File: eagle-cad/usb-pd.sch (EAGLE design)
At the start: 41 parts, among them Q1 CERAMIC_RESONATOR_SMD6M00G53Z, U1 ATMEGA328-AU

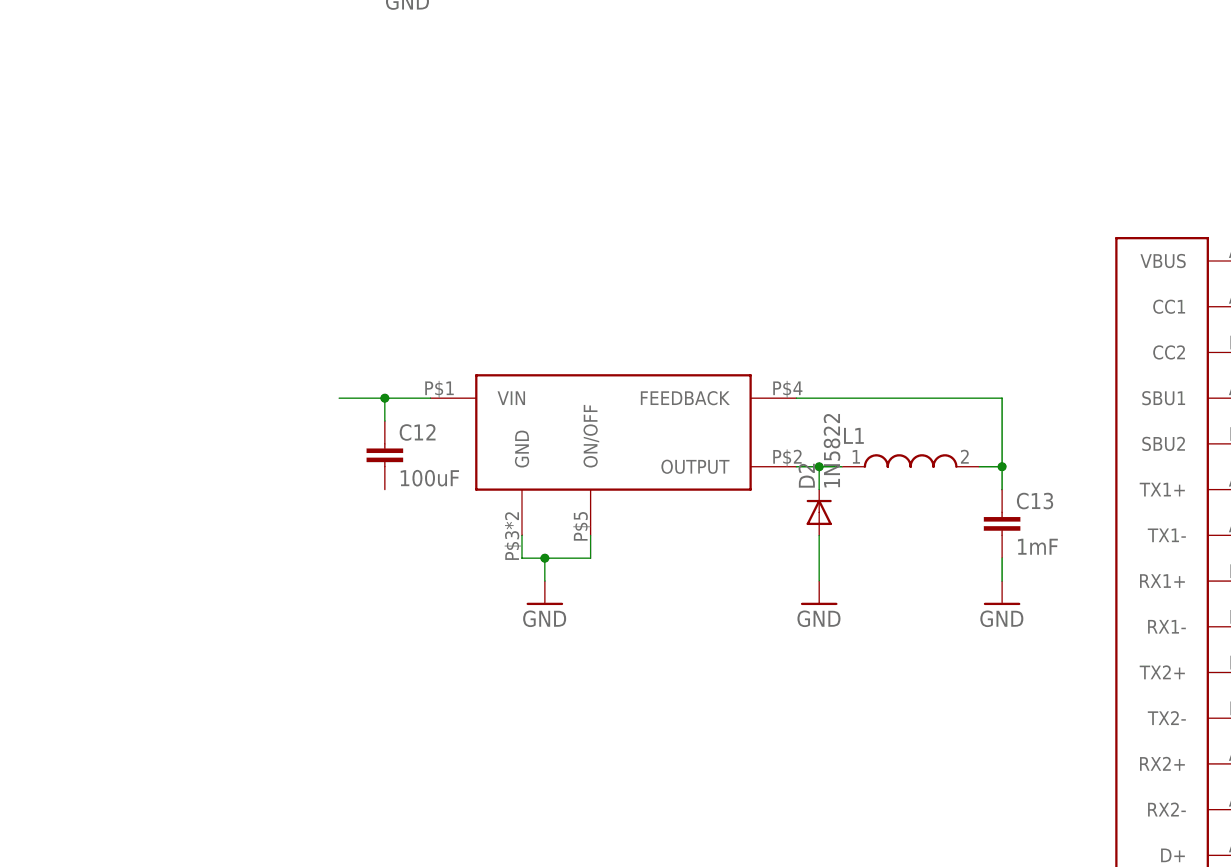
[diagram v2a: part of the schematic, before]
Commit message: Added a n-channel power MOSFET to serve as controlling power FET for 5V buck. Definitely needs review
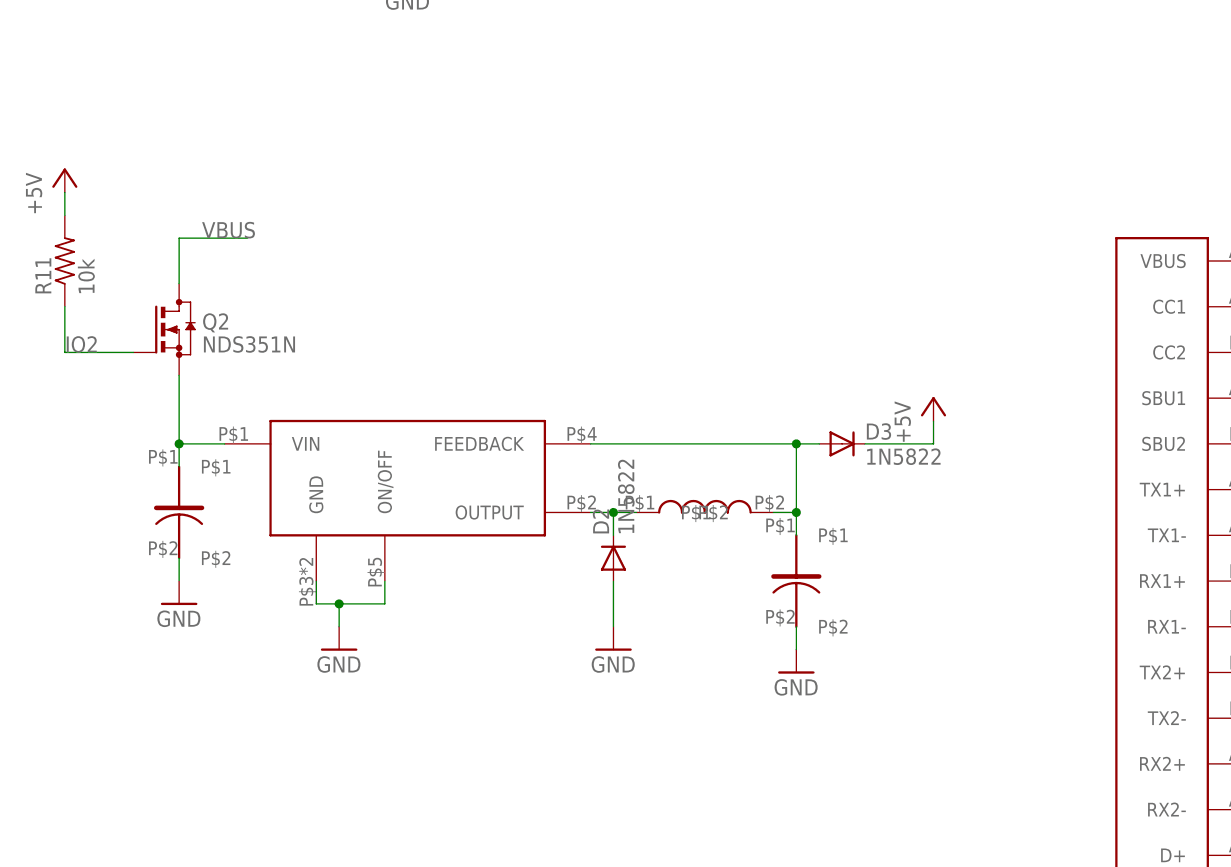
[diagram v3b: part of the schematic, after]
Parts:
- removed C12: 100uF, rcl:C-EUC0805
- removed L1: (no value), EagleLibrary_Wuerth_Elektronik_eiSos_rev16a:WE-RFI_0805
- added D3: 1N5822, diode:1N5400
- added Q2: NDS351N, transistor-small-signal:BSS123
- added R11: 10k, rcl:R-US_R0805
- added U$7: WEURTH-784771101, usb-pd:WEURTH-784771101
- added U$8: UWT1V101MCL1GS, usb-pd:UWT1V101MCL1GS
- C13: value 1mF -> AVE108M10G24T-F; device rcl:C-EUC0805 -> usb-pd:AVE108M10G24T-F
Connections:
- net +5V: now also D3.C, R11.2
- net GND: now also C13.P$2, U$8.P$2; no longer C13.2
- net IO2: now also Q2.G, R11.1
- net N$1: now also Q2.S, U$8.P$1; no longer C12.1
- net N$15: now also C13.P$1, D3.A, U$7.P$2; no longer C13.1, L1.2
- net N$9: now also U$7.P$1; no longer L1.1
- net VBUS: now also Q2.D
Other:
- moved on the sheet: D2
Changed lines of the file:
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@@
 <part name="+3V3" library="supply1" deviceset="+3V3" device=""/>
 <part name="U$6" library="usb-pd" deviceset="TI-LM2576-5.0" device=""/>
-<part name="C12" library="rcl" deviceset="C-EU" device="C0805" value="100uF"/>
 <part name="GND17" library="supply1" deviceset="GND" device=""/>
-<part name="C13" library="rcl" deviceset="C-EU" device="C0805" value="1mF"/>
 <part name="GND18" library="supply1" deviceset="GND" device=""/>
 <part name="D2" library="diode" deviceset="1N5400" device="" value="1N5822"/>
 <part name="GND19" library="supply1" deviceset="GND" device=""/>
-<part name="L1" library="EagleLibrary_Wuerth_Elektronik_eiSos_rev16a" deviceset="WE-RFI" device="_0805"/>
+<part name="D3" library="diode" deviceset="1N5400" device="" value="1N5822"/>
+<part name="P+12" library="supply1" deviceset="+5V" device=""/>
+<part name="U$7" library="usb-pd" deviceset="WEURTH-784771101" device=""/>
+<part name="C13" library="usb-pd" deviceset="AVE108M10G24T-F" device=""/>
+<part name="GND20" library="supply1" deviceset="GND" device=""/>
+<part name="U$8" library="usb-pd" deviceset="UWT1V101MCL1GS" device=""/>
+<part name="Q2" library="transistor-small-signal" deviceset="BSS123" device="" value="NDS351N"/>
+<part name="P+13" library="supply1" deviceset="+5V" device=""/>
+<part name="R11" library="rcl" deviceset="R-US_" device="R0805" value="10k"/>
 </parts>
 <sheets>
@@
 <instance part="P+11" gate="1" x="208.28" y="132.08"/>
 <instance part="+3V3" gate="G$1" x="215.9" y="132.08"/>
-<instance part="U$6" gate="G$1" x="-76.2" y="60.96"/>
-<instance part="C12" gate="G$1" x="-96.52" y="58.42"/>
-<instance part="GND17" gate="1" x="-78.74" y="40.64"/>
-<instance part="C13" gate="G$1" x="-27.94" y="50.8"/>
-<instance part="GND18" gate="1" x="-27.94" y="40.64"/>
-<instance part="D2" gate="1" x="-48.26" y="50.8" rot="R90"/>
-<instance part="GND19" gate="1" x="-48.26" y="40.64"/>
-<instance part="L1" gate="G$1" x="-38.1" y="55.88"/>
+<instance part="U$6" gate="G$1" x="-99.06" y="55.88"/>
+<instance part="GND17" gate="1" x="-101.6" y="35.56"/>
+<instance part="GND18" gate="1" x="-50.8" y="33.02"/>
+<instance part="D2" gate="1" x="-71.12" y="45.72" rot="R90"/>
+<instance part="GND19" gate="1" x="-71.12" y="35.56"/>
+<instance part="D3" gate="1" x="-45.72" y="58.42"/>
+<instance part="P+12" gate="1" x="-35.56" y="63.5"/>
+<instance part="U$7" gate="G$1" x="-60.96" y="50.8"/>
+<instance part="C13" gate="G$1" x="-50.8" y="45.72"/>
+<instance part="GND20" gate="1" x="-119.38" y="40.64"/>
+<instance part="U$8" gate="G$1" x="-119.38" y="53.34"/>
+<instance part="Q2" gate="G$1" x="-119.38" y="71.12"/>
+<instance part="P+13" gate="1" x="-132.08" y="88.9"/>
+<instance part="R11" gate="G$1" x="-132.08" y="78.74" rot="R90"/>
 </instances>
 <busses>
@@
 <wire x1="208.28" y1="124.46" x2="208.28" y2="129.54" width="0.1524" layer="91"/>
 </segment>
+<segment>
+<pinref part="D3" gate="1" pin="C"/>
+<wire x1="-43.18" y1="58.42" x2="-35.56" y2="58.42" width="0.1524" layer="91"/>
+<pinref part="P+12" gate="1" pin="+5V"/>
+<wire x1="-35.56" y1="58.42" x2="-35.56" y2="60.96" width="0.1524" layer="91"/>
+</segment>
+<segment>
+<pinref part="R11" gate="G$1" pin="2"/>
+<pinref part="P+13" gate="1" pin="+5V"/>
+<wire x1="-132.08" y1="83.82" x2="-132.08" y2="86.36" width="0.1524" layer="91"/>
+</segment>
 </net>
 <net name="GND" class="0">
@@
 <segment>
 <pinref part="U$6" gate="G$1" pin="GND"/>
-<wire x1="-81.28" y1="48.26" x2="-81.28" y2="45.72" width="0.1524" layer="91"/>
+<wire x1="-104.14" y1="43.18" x2="-104.14" y2="40.64" width="0.1524" layer="91"/>
 <pinref part="GND17" gate="1" pin="GND"/>
-<wire x1="-81.28" y1="45.72" x2="-78.74" y2="45.72" width="0.1524" layer="91"/>
-<wire x1="-78.74" y1="45.72" x2="-78.74" y2="43.18" width="0.1524" layer="91"/>
-<junction x="-78.74" y="45.72"/>
+<wire x1="-104.14" y1="40.64" x2="-101.6" y2="40.64" width="0.1524" layer="91"/>
+<wire x1="-101.6" y1="40.64" x2="-101.6" y2="38.1" width="0.1524" layer="91"/>
+<junction x="-101.6" y="40.64"/>
 <pinref part="U$6" gate="G$1" pin="ON/OFF"/>
-<wire x1="-73.66" y1="48.26" x2="-73.66" y2="45.72" width="0.1524" layer="91"/>
-<wire x1="-73.66" y1="45.72" x2="-78.74" y2="45.72" width="0.1524" layer="91"/>
+<wire x1="-96.52" y1="43.18" x2="-96.52" y2="40.64" width="0.1524" layer="91"/>
+<wire x1="-96.52" y1="40.64" x2="-101.6" y2="40.64" width="0.1524" layer="91"/>
 </segment>
 <segment>
 <pinref part="GND18" gate="1" pin="GND"/>
-<pinref part="C13" gate="G$1" pin="2"/>
-<wire x1="-27.94" y1="43.18" x2="-27.94" y2="45.72" width="0.1524" layer="91"/>
+<wire x1="-50.8" y1="35.56" x2="-50.8" y2="38.1" width="0.1524" layer="91"/>
+<pinref part="C13" gate="G$1" pin="P$2"/>
 </segment>
 <segment>
 <pinref part="D2" gate="1" pin="A"/>
 <pinref part="GND19" gate="1" pin="GND"/>
-<wire x1="-48.26" y1="48.26" x2="-48.26" y2="43.18" width="0.1524" layer="91"/>
+<wire x1="-71.12" y1="43.18" x2="-71.12" y2="38.1" width="0.1524" layer="91"/>
+</segment>
+<segment>
+<pinref part="GND20" gate="1" pin="GND"/>
+<wire x1="-119.38" y1="43.18" x2="-119.38" y2="45.72" width="0.1524" layer="91"/>
+<pinref part="U$8" gate="G$1" pin="P$2"/>
 </segment>
 </net>
@@
 <label x="198.12" y="15.24" size="1.778" layer="95"/>
 </segment>
+<segment>
+<pinref part="R11" gate="G$1" pin="1"/>
+<wire x1="-132.08" y1="73.66" x2="-132.08" y2="68.58" width="0.1524" layer="91"/>
+<pinref part="Q2" gate="G$1" pin="G"/>
+<wire x1="-132.08" y1="68.58" x2="-124.46" y2="68.58" width="0.1524" layer="91"/>
+<label x="-132.08" y="68.58" size="1.778" layer="95"/>
+</segment>
 </net>
 <net name="IO3" class="0">
@@
 <label x="218.44" y="116.84" size="1.778" layer="95"/>
 </segment>
+<segment>
+<pinref part="Q2" gate="G$1" pin="D"/>
+<wire x1="-119.38" y1="76.2" x2="-119.38" y2="81.28" width="0.1524" layer="91"/>
+<wire x1="-119.38" y1="81.28" x2="-111.76" y2="81.28" width="0.1524" layer="91"/>
+<label x="-116.84" y="81.28" size="1.778" layer="95"/>
+</segment>
 </net>
 <net name="N$1" class="0">
 <segment>
 <pinref part="U$6" gate="G$1" pin="VIN"/>
-<pinref part="C12" gate="G$1" pin="1"/>
-<wire x1="-91.44" y1="63.5" x2="-96.52" y2="63.5" width="0.1524" layer="91"/>
-<wire x1="-96.52" y1="63.5" x2="-96.52" y2="60.96" width="0.1524" layer="91"/>
-<wire x1="-96.52" y1="63.5" x2="-101.6" y2="63.5" width="0.1524" layer="91"/>
-<junction x="-96.52" y="63.5"/>
+<wire x1="-114.3" y1="58.42" x2="-119.38" y2="58.42" width="0.1524" layer="91"/>
+<pinref part="U$8" gate="G$1" pin="P$1"/>
+<wire x1="-119.38" y1="55.88" x2="-119.38" y2="58.42" width="0.1524" layer="91"/>
+<pinref part="Q2" gate="G$1" pin="S"/>
+<wire x1="-119.38" y1="58.42" x2="-119.38" y2="66.04" width="0.1524" layer="91"/>
+<junction x="-119.38" y="58.42"/>
 </segment>
 </net>
 <net name="N$15" class="0">
 <segment>
-<pinref part="C13" gate="G$1" pin="1"/>
-<wire x1="-27.94" y1="55.88" x2="-27.94" y2="53.34" width="0.1524" layer="91"/>
-<junction x="-27.94" y="55.88"/>
+<wire x1="-50.8" y1="50.8" x2="-50.8" y2="48.26" width="0.1524" layer="91"/>
+<junction x="-50.8" y="50.8"/>
 <pinref part="U$6" gate="G$1" pin="FEEDBACK"/>
-<wire x1="-50.8" y1="63.5" x2="-27.94" y2="63.5" width="0.1524" layer="91"/>
-<wire x1="-27.94" y1="63.5" x2="-27.94" y2="55.88" width="0.1524" layer="91"/>
-<pinref part="L1" gate="G$1" pin="2"/>
-<wire x1="-30.48" y1="55.88" x2="-27.94" y2="55.88" width="0.1524" layer="91"/>
+<wire x1="-73.66" y1="58.42" x2="-50.8" y2="58.42" width="0.1524" layer="91"/>
+<wire x1="-50.8" y1="58.42" x2="-50.8" y2="50.8" width="0.1524" layer="91"/>
+<wire x1="-53.34" y1="50.8" x2="-50.8" y2="50.8" width="0.1524" layer="91"/>
+<junction x="-50.8" y="58.42"/>
+<pinref part="D3" gate="1" pin="A"/>
+<wire x1="-48.26" y1="58.42" x2="-50.8" y2="58.42" width="0.1524" layer="91"/>
+<pinref part="U$7" gate="G$1" pin="P$2"/>
+<pinref part="C13" gate="G$1" pin="P$1"/>
 </segment>
 </net>
@@
 <pinref part="U$6" gate="G$1" pin="OUTPUT"/>
 <pinref part="D2" gate="1" pin="C"/>
-<wire x1="-50.8" y1="55.88" x2="-48.26" y2="55.88" width="0.1524" layer="91"/>
-<wire x1="-48.26" y1="55.88" x2="-48.26" y2="53.34" width="0.1524" layer="91"/>
-<junction x="-48.26" y="55.88"/>
-<pinref part="L1" gate="G$1" pin="1"/>
-<wire x1="-48.26" y1="55.88" x2="-45.72" y2="55.88" width="0.1524" layer="91"/>
-</segment>
-</net>
+<wire x1="-73.66" y1="50.8" x2="-71.12" y2="50.8" width="0.1524" layer="91"/>
+<wire x1="-71.12" y1="50.8" x2="-71.12" y2="48.26" width="0.1524" layer="91"/>
+<junction x="-71.12" y="50.8"/>
+<wire x1="-71.12" y1="50.8" x2="-68.58" y2="50.8" width="0.1524" layer="91"/>
+<pinref part="U$7" gate="G$1" pin="P$1"/>
+</segment>
+</net>

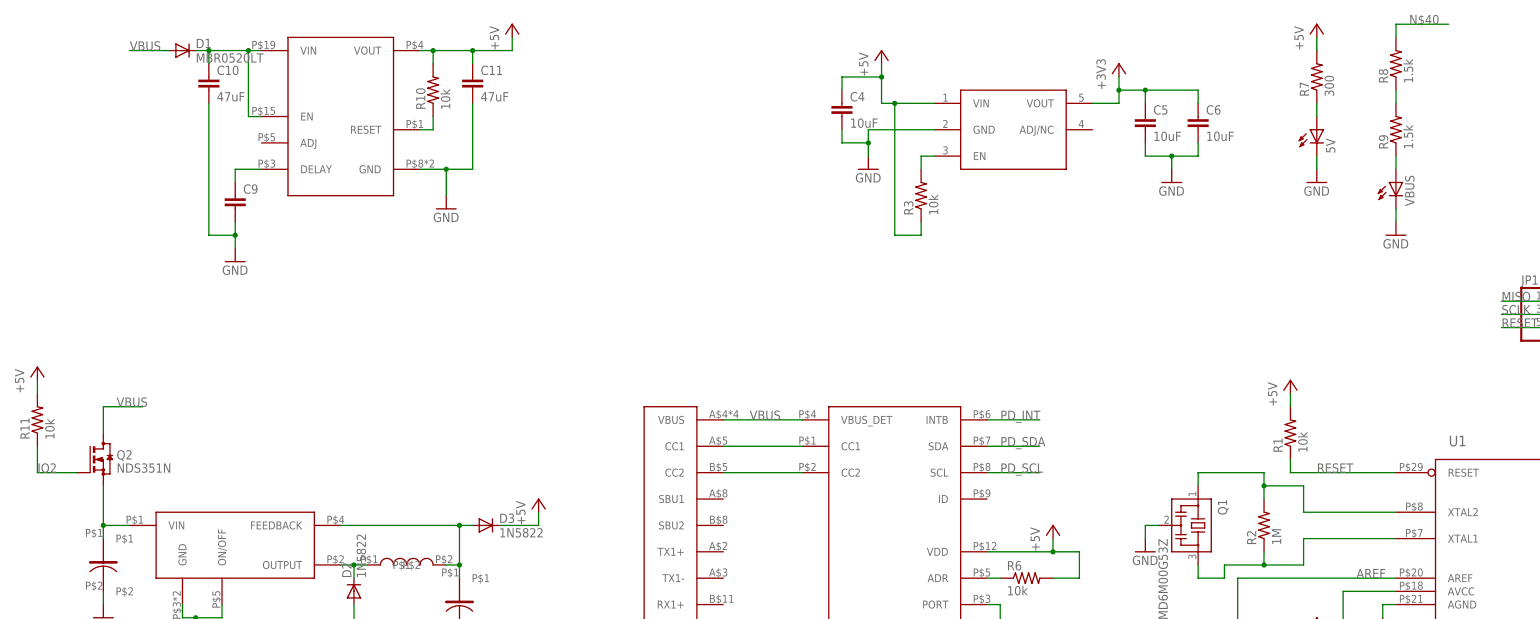
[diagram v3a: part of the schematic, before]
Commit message: switched to p-channel because I'm dumb
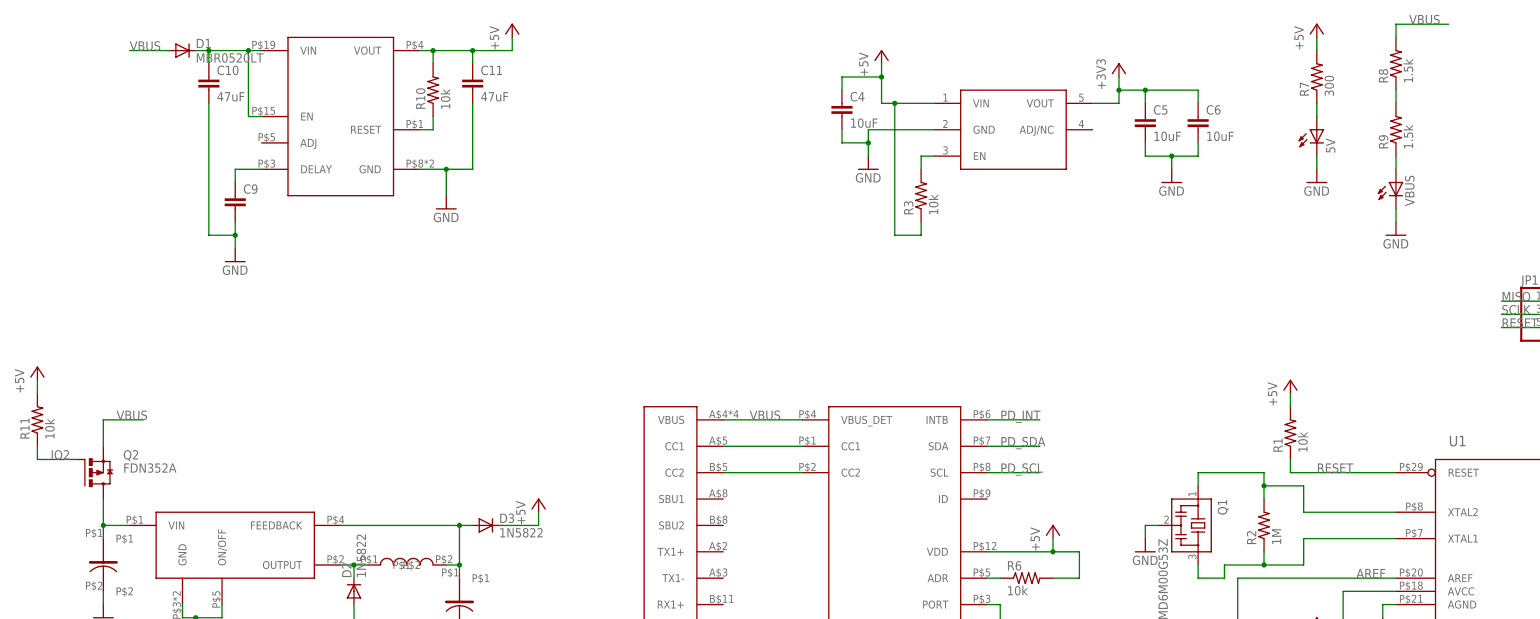
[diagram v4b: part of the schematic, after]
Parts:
- Q2: value NDS351N -> FDN352A; device transistor-small-signal:BSS123 -> transistor-power:FDN360P
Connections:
- net N$1: now also Q2.D; no longer Q2.S
- net N$40: no longer R8.2
- net VBUS: now also Q2.S, R8.2; no longer Q2.D
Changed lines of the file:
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@@
 <part name="GND20" library="supply1" deviceset="GND" device=""/>
 <part name="U$8" library="usb-pd" deviceset="UWT1V101MCL1GS" device=""/>
-<part name="Q2" library="transistor-small-signal" deviceset="BSS123" device="" value="NDS351N"/>
 <part name="P+13" library="supply1" deviceset="+5V" device=""/>
 <part name="R11" library="rcl" deviceset="R-US_" device="R0805" value="10k"/>
+<part name="Q2" library="transistor-power" deviceset="FDN360P" device="" value="FDN352A"/>
 </parts>
 <sheets>
@@
 <instance part="GND20" gate="1" x="-119.38" y="40.64"/>
 <instance part="U$8" gate="G$1" x="-119.38" y="53.34"/>
-<instance part="Q2" gate="G$1" x="-119.38" y="71.12"/>
 <instance part="P+13" gate="1" x="-132.08" y="88.9"/>
 <instance part="R11" gate="G$1" x="-132.08" y="78.74" rot="R90"/>
+<instance part="Q2" gate="G$1" x="-121.92" y="68.58"/>
 </instances>
 <busses>
@@
 <net name="N$40" class="0">
 <segment>
-<pinref part="R8" gate="G$1" pin="2"/>
-<wire x1="129.54" y1="152.4" x2="129.54" y2="154.94" width="0.1524" layer="91"/>
-<wire x1="129.54" y1="154.94" x2="139.7" y2="154.94" width="0.1524" layer="91"/>
-<label x="132.08" y="154.94" size="1.778" layer="95"/>
-</segment>
-<segment>
 <pinref part="U$2" gate="G$1" pin="VIN"/>
 <wire x1="-88.9" y1="149.86" x2="-91.44" y2="149.86" width="0.1524" layer="91"/>
@@
 <segment>
 <pinref part="R11" gate="G$1" pin="1"/>
-<wire x1="-132.08" y1="73.66" x2="-132.08" y2="68.58" width="0.1524" layer="91"/>
+<wire x1="-132.08" y1="73.66" x2="-132.08" y2="71.12" width="0.1524" layer="91"/>
+<wire x1="-132.08" y1="71.12" x2="-124.46" y2="71.12" width="0.1524" layer="91"/>
+<label x="-129.54" y="71.12" size="1.778" layer="95"/>
 <pinref part="Q2" gate="G$1" pin="G"/>
-<wire x1="-132.08" y1="68.58" x2="-124.46" y2="68.58" width="0.1524" layer="91"/>
-<label x="-132.08" y="68.58" size="1.778" layer="95"/>
 </segment>
 </net>
@@
 </segment>
 <segment>
-<pinref part="Q2" gate="G$1" pin="D"/>
-<wire x1="-119.38" y1="76.2" x2="-119.38" y2="81.28" width="0.1524" layer="91"/>
-<wire x1="-119.38" y1="81.28" x2="-111.76" y2="81.28" width="0.1524" layer="91"/>
-<label x="-116.84" y="81.28" size="1.778" layer="95"/>
+<wire x1="-119.38" y1="73.66" x2="-119.38" y2="78.74" width="0.1524" layer="91"/>
+<wire x1="-119.38" y1="78.74" x2="-111.76" y2="78.74" width="0.1524" layer="91"/>
+<label x="-116.84" y="78.74" size="1.778" layer="95"/>
+<pinref part="Q2" gate="G$1" pin="S"/>
+</segment>
+<segment>
+<pinref part="R8" gate="G$1" pin="2"/>
+<wire x1="129.54" y1="152.4" x2="129.54" y2="154.94" width="0.1524" layer="91"/>
+<wire x1="129.54" y1="154.94" x2="139.7" y2="154.94" width="0.1524" layer="91"/>
+<label x="132.08" y="154.94" size="1.778" layer="95"/>
 </segment>
 </net>
@@
 <pinref part="U$8" gate="G$1" pin="P$1"/>
 <wire x1="-119.38" y1="55.88" x2="-119.38" y2="58.42" width="0.1524" layer="91"/>
-<pinref part="Q2" gate="G$1" pin="S"/>
-<wire x1="-119.38" y1="58.42" x2="-119.38" y2="66.04" width="0.1524" layer="91"/>
+<wire x1="-119.38" y1="58.42" x2="-119.38" y2="63.5" width="0.1524" layer="91"/>
 <junction x="-119.38" y="58.42"/>
-</segment>
-</net>
+<pinref part="Q2" gate="G$1" pin="D"/>
+</segment>
+</net>
